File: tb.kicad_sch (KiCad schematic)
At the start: 67 parts, among them U4 JHL6340SLLSQ, U5 MX25L8006EM1I-12G, U6 SI52112-B6-GT, U7 MX25L8006EM2I-12G, Y1 Resonator_25MHz_ABM8G, Y2 Resonator_25MHz_ABM8G

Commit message: [#61922] Update LT8350RV#PBF symbol
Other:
- moved on the sheet: C102, C103, C104, C105, C106, C107, C108, C109, C110, C111, C112, C113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

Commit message: [#61922] Update all symbols, clean ERC
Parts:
- C100, C101, C102, C103, C104, C105, C106, C107, C108, C109, C110, C111, C112, C113, C114, C115, C116, C117, C98, C99, R50, R51, R52, R53, R54, R55, R56, R57, R58, R59, R60, R61, R62, R64, R65, R66, R67, R68, R69, R70, R71, R72, R73, R74, R75, R77, R78, R79, R80, R81, R82, R83, R84, R85, R86, R87, R88, R89, R90, Y1, Y2: Public (none) -> False
- R63, R76: DNP DNP -> (none); Public (none) -> False; now in the parts list
- U7: DNP DNP -> (none); now in the parts list

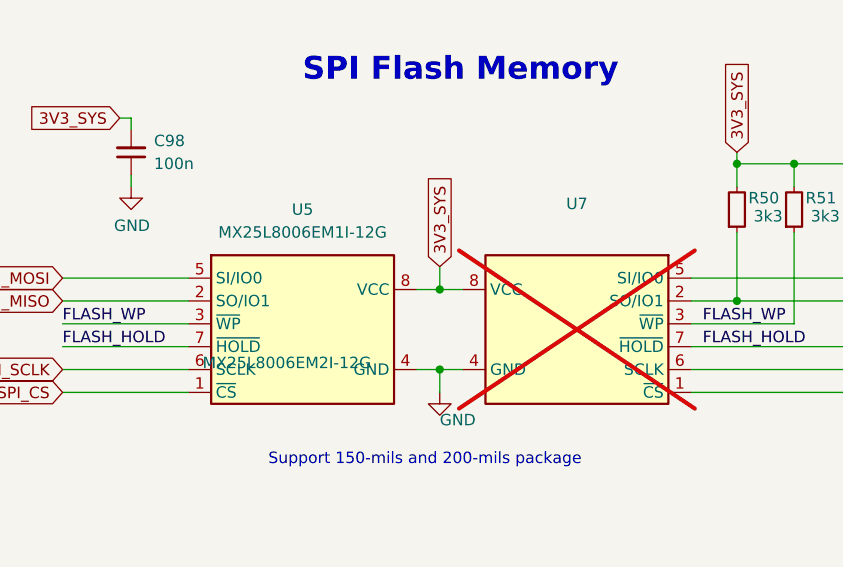
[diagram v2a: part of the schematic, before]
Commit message: [#61922] Update all footprints, clean DRC errors
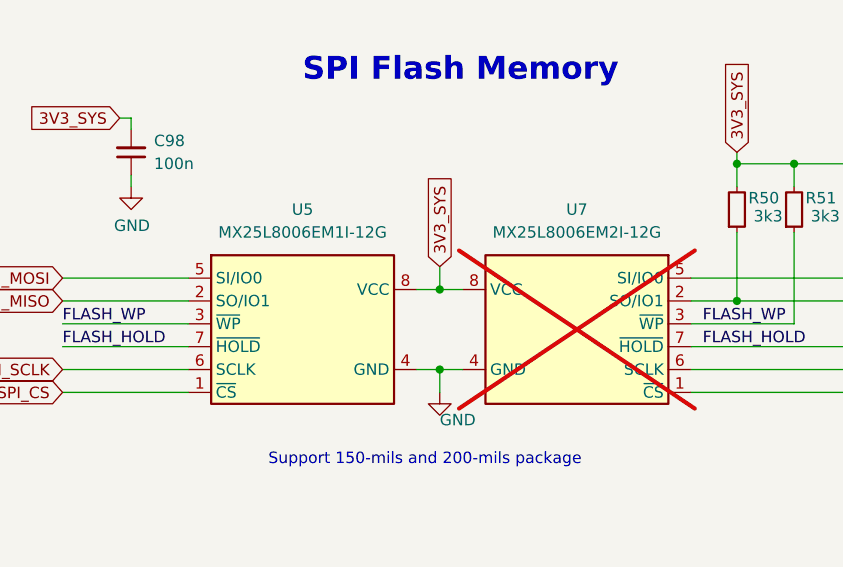
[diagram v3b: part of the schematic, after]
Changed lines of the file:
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@@
   )
   (symbol (lib_id "antmicroMemory:MX25L8006EM2I-12G") (at 294.64 229.87 0) (mirror y) (unit 1)
-    (in_bom yes) (on_board yes) (dnp yes)
-    (property "Reference" "U7" (at 281.94 221.615 0)
+    (in_bom yes) (on_board yes) (dnp yes) (fields_autoplaced)
+    (property "Reference" "U7" (at 281.94 222.25 0)
       (effects (font (size 1.27 1.27) (thickness 0.15)))
     )
@@
       (effects (font (size 1.27 1.27) (thickness 0.15)) (justify left bottom) hide)
     )
-    (property "MPN" "MX25L8006EM2I-12G" (at 259.08 240.03 0)
-      (effects (font (size 1.27 1.27) (thickness 0.15)) (justify left bottom))
+    (property "MPN" "MX25L8006EM2I-12G" (at 281.94 224.79 0)
+      (effects (font (size 1.27 1.27) (thickness 0.15)))
     )
     (property "Manufacturer" "Macronix" (at 259.08 242.57 0)

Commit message: [#61922] Perform kmake dnp & update symbols
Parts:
- C100, C101, C102, C103, C104, C105, C106, C107, C108, C109, C110, C111, C112, C113, C114, C115, C116, C117, C98, C99, R50, R51, R52, R53, R54, R55, R56, R57, R58, R59, R60, R61, R62, R63, R64, R65, R66, R67, R68, R69, R70, R71, R72, R73, R74, R75, R76, R77, R78, R79, R80, R81, R82, R83, R84, R85, R86, R87, R88, R89, R90, Y1, Y2: Public False -> (none)
